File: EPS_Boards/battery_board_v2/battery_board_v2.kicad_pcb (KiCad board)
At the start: 4 copper layers, 90.2 x 95.9 mm, 5 parts, among them J1 PC104_Connector

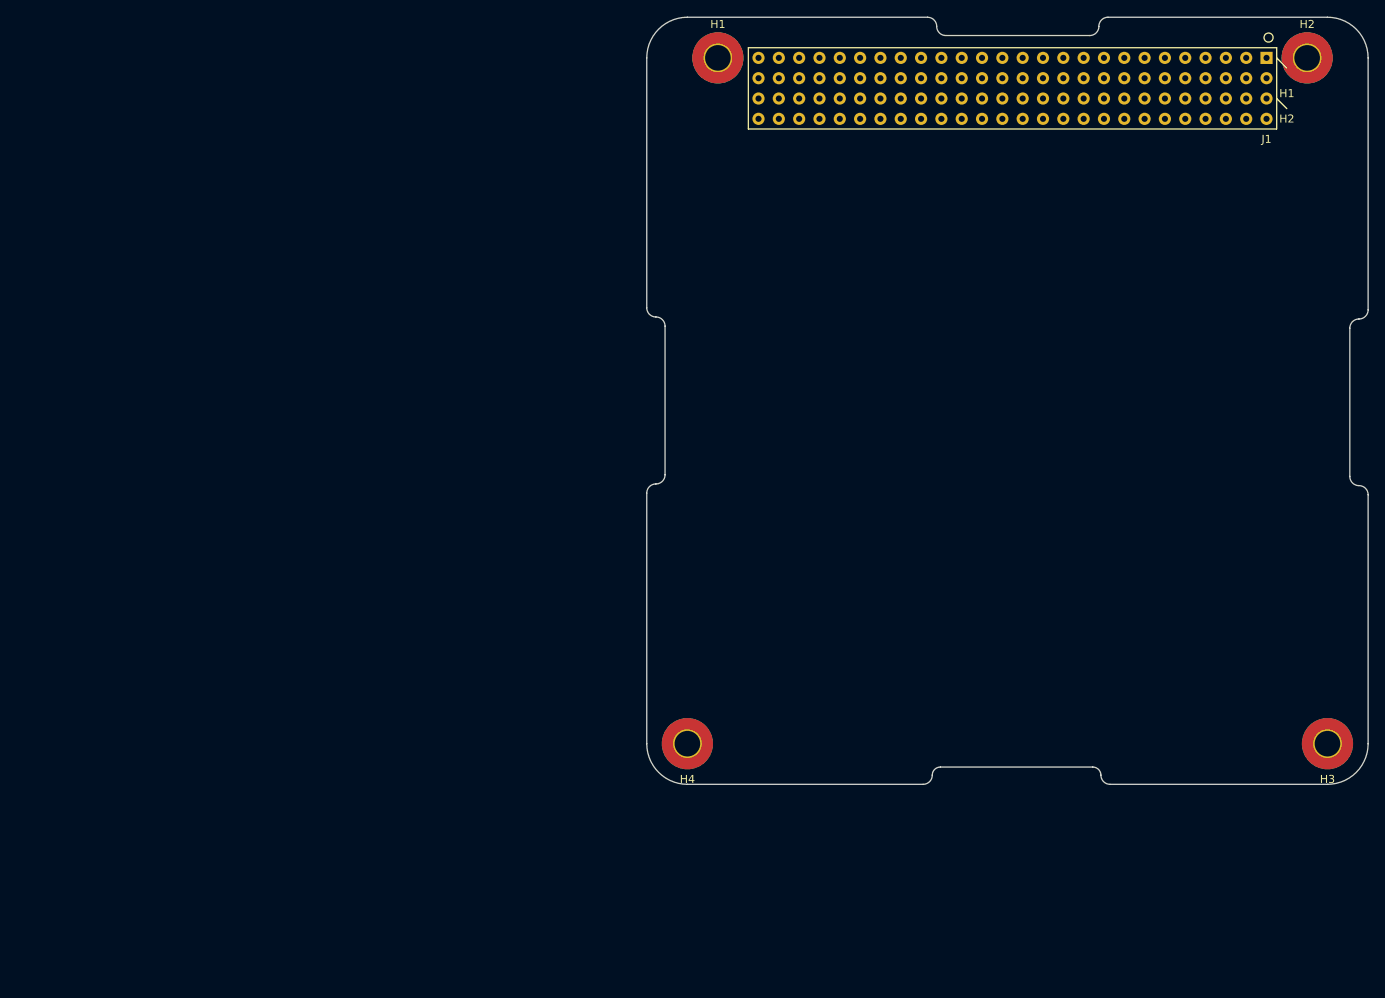
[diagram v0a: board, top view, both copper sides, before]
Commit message: eps: battery board: updated board layout
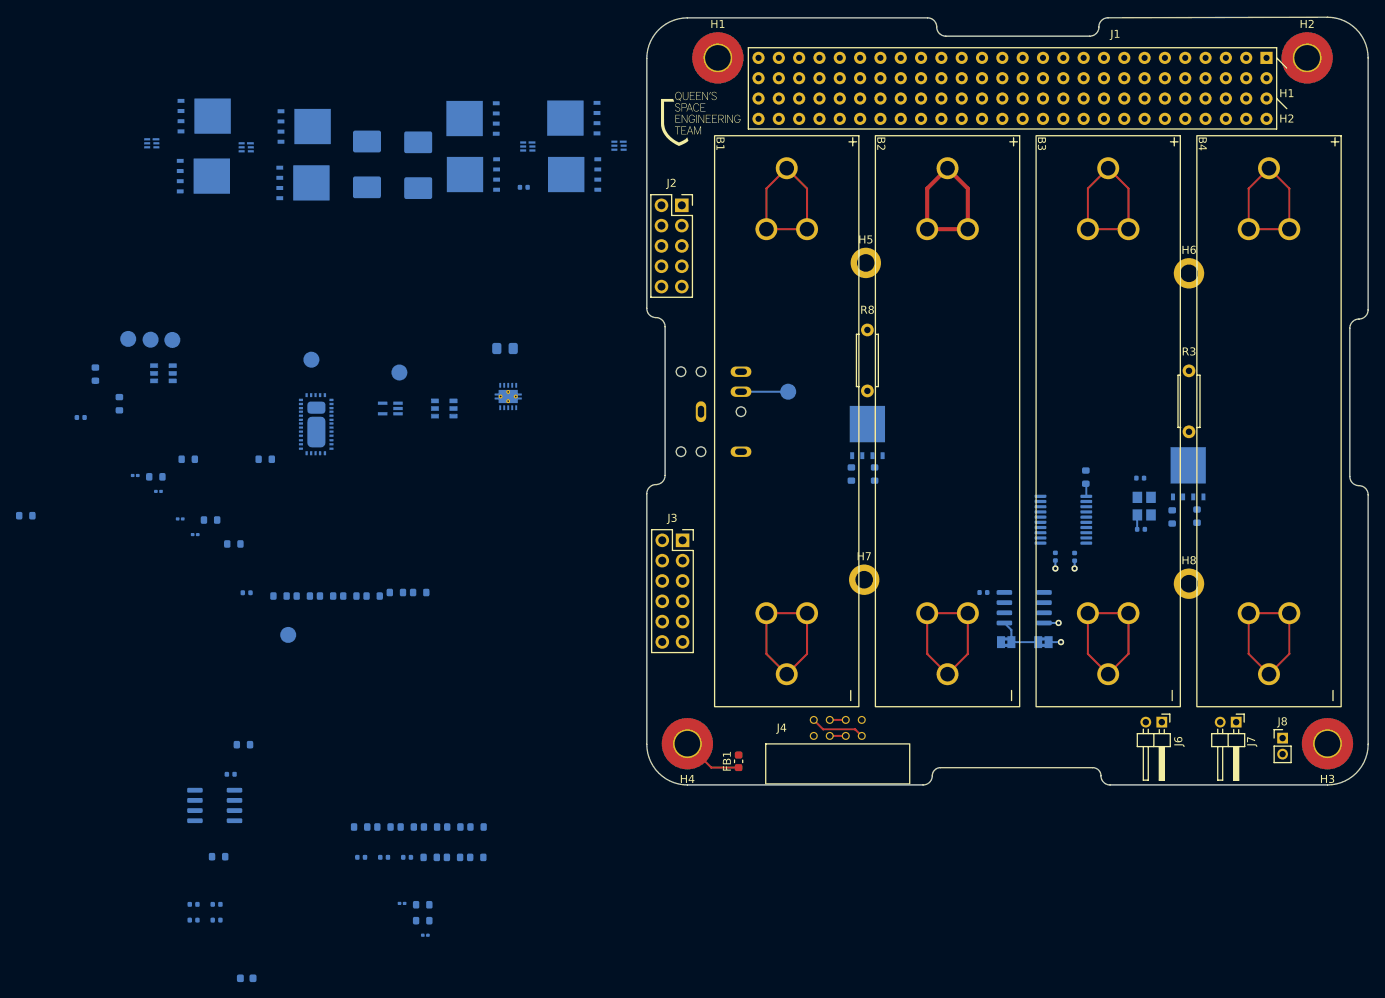
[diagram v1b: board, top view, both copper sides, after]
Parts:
- added B1: NCR18650GA, qset-footprints:Keystone_54_18650, F.Cu at (117.7, 61.8)
- added B2: NCR18650GA, qset-footprints:Keystone_54_18650, F.Cu at (137.8, 61.8)
- added B3: NCR18650GA, qset-footprints:Keystone_54_18650, F.Cu at (157.9, 61.8)
- added B4: NCR18650GA, qset-footprints:Keystone_54_18650, F.Cu at (178.0, 61.8)
- added C1: 0.1u, Capacitor_SMD:C_0402_1005Metric, B.Cu at (151.3, 118.9)
- added C10: 0.1u, Capacitor_SMD:C_0201_0603Metric, B.Cu at (48.2, 106.3)
- added C11: 0.1u, Capacitor_SMD:C_0402_1005Metric, B.Cu at (59.2, 118.9)
- added C12: C, Capacitor_SMD:C_0201_0603Metric, B.Cu at (45.3, 104.3)
- added C13: 0.1u, Capacitor_SMD:C_0201_0603Metric, B.Cu at (50.9, 109.7)
- added C14: 0.1u, Capacitor_SMD:C_0402_1005Metric, B.Cu at (38.5, 97.0)
- added C15: 0.1u, Capacitor_SMD:C_0201_0603Metric, B.Cu at (52.8, 111.7)
- added C16: 0.1u, Capacitor_SMD:C_0402_1005Metric, B.Cu at (76.4, 152.0)
- added C17: 0.1u, Capacitor_SMD:C_0402_1005Metric, B.Cu at (93.8, 68.2)
- added C18: 0.1u, Capacitor_SMD:C_0402_1005Metric, B.Cu at (73.5, 152.0)
- added C19: 0.1u, Capacitor_SMD:C_0402_1005Metric, B.Cu at (79.3, 152.0)
- added C2: 10p, Capacitor_SMD:C_0402_1005Metric, B.Cu at (170.9, 104.6)
- added C20: 0.1u, Capacitor_SMD:C_0402_1005Metric, B.Cu at (57.2, 141.6)
- added C21: 0.1u, Capacitor_SMD:C_0201_0603Metric, B.Cu at (81.5, 161.7)
- added C22: 22n, Capacitor_SMD:C_0201_0603Metric, B.Cu at (78.6, 157.8)
- added C3: 100u, Capacitor_SMD:C_0402_1005Metric, B.Cu at (55.4, 159.8)
- added C4: 10p, Capacitor_SMD:C_0402_1005Metric, B.Cu at (171.0, 111.0)
- added C5: 10u, Capacitor_SMD:C_0402_1005Metric, B.Cu at (160.3, 114.4)
- added C6: 100n, Capacitor_SMD:C_0402_1005Metric, B.Cu at (162.7, 114.4)
- added C7: 10n, Capacitor_SMD:C_0402_1005Metric, B.Cu at (55.4, 157.9)
- added C8: 1u, Capacitor_SMD:C_0402_1005Metric, B.Cu at (52.6, 159.8)
- added C9: 1u, Capacitor_SMD:C_0402_1005Metric, B.Cu at (52.6, 157.9)
- added F1: Polyfuse, Capacitor_Tantalum_SMD:CP_EIA-7132-20_AVX-U_Pad2.72x3.50mm_HandSolder, B.Cu at (80.7, 65.5)
- added F2: Polyfuse, Capacitor_Tantalum_SMD:CP_EIA-7132-20_AVX-U_Pad2.72x3.50mm_HandSolder, B.Cu at (74.2, 65.4)
- added FB1: FerriteBead, Inductor_SMD:L_0603_1608Metric, F.Cu at (120.7, 140.0)
- added FB2: 100R @ 100MHz, Inductor_SMD:L_0603_1608Metric, B.Cu at (59.2, 167.1)
- added G***: LOGO, qset-footprints:Logo-10mm, F.Cu at (116.0, 59.6)
- added H5: MountingHole, MountingHole:MountingHole_2.2mm_M2_DIN965_Pad, F.Cu at (136.6, 77.7)
- added H6: MountingHole, MountingHole:MountingHole_2.2mm_M2_DIN965_Pad, F.Cu at (177.0, 79.0)
- added H7: MountingHole, MountingHole:MountingHole_2.2mm_M2_DIN965_Pad, F.Cu at (136.4, 117.3)
- added H8: MountingHole, MountingHole:MountingHole_2.2mm_M2_DIN965_Pad, F.Cu at (177.0, 117.8)
- added J2: Programming Header, Connector_PinSocket_2.54mm:PinSocket_2x05_P2.54mm_Vertical, F.Cu at (113.6, 70.5)
- added J3: System Test Connector, Connector_PinSocket_2.54mm:PinSocket_2x06_P2.54mm_Vertical, F.Cu at (113.7, 112.4)
- added J4: Conn_01x08_Male, qset-footprints:M80-5300842, F.Cu at (124.1, 142.8)
- added J5: RBF, qset-footprints:CUI_SJ1-3524NG, B.Cu at (116.0, 96.3)
- added J6: RBF Deployment Bypass, Connector_PinHeader_2.00mm:PinHeader_1x02_P2.00mm_Horizontal, F.Cu at (173.6, 135.1)
- added J7: 30s Timer, Connector_PinHeader_2.00mm:PinHeader_1x02_P2.00mm_Horizontal, F.Cu at (182.9, 135.1)
- added J8: Shunt Resistor, Connector_PinHeader_2.00mm:PinHeader_1x02_P2.00mm_Vertical, F.Cu at (188.7, 137.1)
- added L1: 2.2uH, Inductor_SMD:L_0805_2012Metric_Pad1.15x1.40mm_HandSolder, B.Cu at (91.5, 88.4)
- added Q1: CSD16401Q5, Package_TO_SOT_SMD:TDSON-8-1, B.Cu at (176.9, 104.0)
- added Q10: CSD16401Q5, Package_TO_SOT_SMD:TDSON-8-1, B.Cu at (53.8, 66.8)
- added Q2: CSD16401Q5, Package_TO_SOT_SMD:TDSON-8-1, B.Cu at (136.8, 98.9)
- added Q3: CSD16401Q5, Package_TO_SOT_SMD:TDSON-8-1, B.Cu at (100.2, 66.7)
- added Q4: CSD16401Q5, Package_TO_SOT_SMD:TDSON-8-1, B.Cu at (87.5, 66.7)
- added Q5: CSD16401Q5, Package_TO_SOT_SMD:TDSON-8-1, B.Cu at (100.1, 59.6)
- added Q6: CSD16401Q5, Package_TO_SOT_SMD:TDSON-8-1, B.Cu at (87.5, 59.6)
- added Q7: CSD16401Q5, Package_TO_SOT_SMD:TDSON-8-1, B.Cu at (66.4, 60.6)
- added Q8: CSD16401Q5, Package_TO_SOT_SMD:TDSON-8-1, B.Cu at (53.9, 59.4)
- added Q9: CSD16401Q5, Package_TO_SOT_SMD:TDSON-8-1, B.Cu at (66.2, 67.7)
- added R1: 100, Resistor_SMD:R_0603_1608Metric, B.Cu at (178.0, 109.3)
- added R10: 412k, Resistor_SMD:R_0603_1608Metric, B.Cu at (54.7, 109.8)
- added R11: 1M, Resistor_SMD:R_0603_1608Metric, B.Cu at (80.8, 118.9)
- added R12: 390k, Resistor_SMD:R_0603_1608Metric, B.Cu at (57.6, 112.8)
- added R13: ?R, Resistor_SMD:R_0603_1608Metric, B.Cu at (31.6, 109.3)
- added R14: 1M, Resistor_SMD:R_0603_1608Metric, B.Cu at (69.2, 119.3)
- added R15: 887k, Resistor_SMD:R_0603_1608Metric, B.Cu at (51.9, 102.2)
- added R16: 0R, Resistor_SMD:R_0603_1608Metric, B.Cu at (66.3, 119.3)
- added R17: DNP, Resistor_SMD:R_0603_1608Metric, B.Cu at (77.9, 118.9)
- added R18: 100k, Resistor_SMD:R_0603_1608Metric, B.Cu at (72.1, 119.3)
- added R19: 100k, Resistor_SMD:R_0603_1608Metric, B.Cu at (43.3, 95.3)
- added R2: 10k, Resistor_SMD:R_0603_1608Metric, B.Cu at (174.9, 109.5)
- added R20: 560k, Resistor_SMD:R_0603_1608Metric, B.Cu at (61.5, 102.2)
- added R21: 100k, Resistor_SMD:R_0603_1608Metric, B.Cu at (47.9, 104.4)
- added R22: 100k, Resistor_SMD:R_0603_1608Metric, B.Cu at (75.0, 119.3)
- added R23: 270k, Resistor_SMD:R_0603_1608Metric, B.Cu at (40.3, 91.6)
- added R24: 100k, Resistor_SMD:R_0603_1608Metric, B.Cu at (63.4, 119.3)
- added R25: 330, Resistor_SMD:R_0603_1608Metric, B.Cu at (73.5, 148.2)
- added R26: 330, Resistor_SMD:R_0603_1608Metric, B.Cu at (79.3, 148.2)
- added R27: 2.2k, Resistor_SMD:R_0603_1608Metric, B.Cu at (82.2, 152.0)
- added R28: 2.2k, Resistor_SMD:R_0603_1608Metric, B.Cu at (88.0, 148.2)
- added R29: 0.1, Resistor_SMD:R_0603_1608Metric, B.Cu at (76.4, 148.2)
- added R3: 100, Resistor_THT:R_Axial_DIN0207_L6.3mm_D2.5mm_P7.62mm_Horizontal, F.Cu at (177.0, 98.8)
- added R30: 2.2k, Resistor_SMD:R_0603_1608Metric, B.Cu at (88.0, 152.0)
- added R31: 2.2k, Resistor_SMD:R_0603_1608Metric, B.Cu at (85.1, 152.0)
- added R32: 330, Resistor_SMD:R_0603_1608Metric, B.Cu at (85.1, 148.2)
- added R33: 330, Resistor_SMD:R_0603_1608Metric, B.Cu at (82.2, 148.2)
- added R34: 3.3k, Resistor_SMD:R_0603_1608Metric, B.Cu at (58.8, 137.9)
- added R35: 3.3k, Resistor_SMD:R_0603_1608Metric, B.Cu at (55.7, 151.9)
- added R36: 10k, Resistor_SMD:R_0603_1608Metric, B.Cu at (81.2, 157.9)
- added R37: 1k, Resistor_SMD:R_0603_1608Metric, B.Cu at (81.2, 159.9)
- added R4: 0R, Jumper:SolderJumper-2_P1.3mm_Bridged2Bar_Pad1.0x1.5mm, B.Cu at (154.2, 125.1)
- added R5: 0R, Jumper:SolderJumper-2_P1.3mm_Bridged2Bar_Pad1.0x1.5mm, B.Cu at (158.8, 125.1)
- added R6: 100, Resistor_SMD:R_0603_1608Metric, B.Cu at (137.7, 104.1)
- added R7: 10k, Resistor_SMD:R_0603_1608Metric, B.Cu at (134.8, 104.1)
- added R8: 100, Resistor_THT:R_Axial_DIN0207_L6.3mm_D2.5mm_P7.62mm_Horizontal, F.Cu at (136.8, 93.7)
- added R9: 10k, Resistor_SMD:R_0603_1608Metric, B.Cu at (164.1, 104.5)
- added TP1: Deployment TP, TestPoint:TestPoint_Pad_D2.0mm, B.Cu at (126.9, 93.8)
- added TP2: Power Control TP, TestPoint:TestPoint_Pad_D2.0mm, B.Cu at (44.4, 87.2)
- added TP3: EN_D3, TestPoint:TestPoint_Pad_D2.0mm, B.Cu at (78.3, 91.4)
- added TP4: Timer, TestPoint:TestPoint_Pad_D2.0mm, B.Cu at (47.2, 87.3)
- added TP5: HB, TestPoint:TestPoint_Pad_D2.0mm, B.Cu at (64.4, 124.2)
- added TP6: EN_D1, TestPoint:TestPoint_Pad_D2.0mm, B.Cu at (67.3, 89.8)
- added TP7: HB Reset, TestPoint:TestPoint_Pad_D2.0mm, B.Cu at (49.9, 87.3)
- added U1: TMP36xS, Package_SO:SOIC-8_3.9x4.9mm_P1.27mm, B.Cu at (156.4, 120.8)
- added U10: BQ297xx, Package_SON:WSON-6_1.5x1.5mm_P0.5mm, B.Cu at (59.1, 63.2)
- added U11: BQ297xx, Package_SON:WSON-6_1.5x1.5mm_P0.5mm, B.Cu at (47.4, 62.8)
- added U12: INA219AxD, Package_SO:SOIC-8_3.9x4.9mm_P1.27mm, B.Cu at (55.2, 145.5)
- added U13: TPS24750, qset-footprints:TPS24750, B.Cu at (67.7, 98.1)
- added U2: STM32F030F4Px, Package_SO:TSSOP-20_4.4x6.5mm_P0.65mm, B.Cu at (161.3, 109.8)
- added U3: TPS63000-Q1, Package_SON:Texas_DRC0010J_ThermalVias, B.Cu at (91.9, 94.4)
- added U4: LTC6995HS6-1#TRMPBF, qset-footprints:SOT95P280X100-6N, B.Cu at (83.9, 95.9)
- added U5: LTC6995HS6-1#TRMPBF, qset-footprints:SOT95P280X100-6N, B.Cu at (48.8, 91.5)
- added U6: 74AUP1G08, qset-footprints:SOT65P210X110-5N, B.Cu at (77.2, 95.9)
- added U8: BQ297xx, Package_SON:WSON-6_1.5x1.5mm_P0.5mm, B.Cu at (105.8, 63.0)
- added U9: BQ297xx, Package_SON:WSON-6_1.5x1.5mm_P0.5mm, B.Cu at (94.3, 63.1)
- added Y1: 16 MHz, Crystal:Crystal_SMD_3225-4Pin_3.2x2.5mm, B.Cu at (171.4, 108.1)
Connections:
- H1 pad 1: unconnected-(H1-Pad1) -> Net-(FB1-Pad1)
- H2 pad 1: unconnected-(H2-Pad1) -> Net-(FB1-Pad1)
- H3 pad 1: unconnected-(H3-Pad1) -> Net-(FB1-Pad1)
- H4 pad 1: unconnected-(H4-Pad1) -> Net-(FB1-Pad1)
- J1 pad 100: unconnected-(J1-Pad100) -> GND
- J1 pad 32: unconnected-(J1-Pad32) -> 5V_USB_CHG
- J1 pad 41: unconnected-(J1-Pad41) -> I2C_DATA
- J1 pad 43: unconnected-(J1-Pad43) -> I2C_CLK
- J1 pad 61: unconnected-(J1-Pad61) -> GND
- J1 pad 66: unconnected-(J1-Pad66) -> GND
- J1 pad 69: unconnected-(J1-Pad69) -> GND
- J1 pad 7: unconnected-(J1-Pad7) -> BAT_INT
- J1 pad 73: unconnected-(J1-Pad73) -> GND
- J1 pad 74: unconnected-(J1-Pad74) -> GND
- J1 pad 77: unconnected-(J1-Pad77) -> 5VBUS
- J1 pad 78: unconnected-(J1-Pad78) -> 5VBUS
- J1 pad 79: unconnected-(J1-Pad79) -> 3V3BUS
- J1 pad 80: unconnected-(J1-Pad80) -> 3V3BUS
- J1 pad 81: unconnected-(J1-Pad81) -> GND
- J1 pad 82: unconnected-(J1-Pad82) -> GND
- J1 pad 84: unconnected-(J1-Pad84) -> GND
- J1 pad 87: unconnected-(J1-Pad87) -> PCM_IN
- J1 pad 88: unconnected-(J1-Pad88) -> PCM_IN
- J1 pad 93: unconnected-(J1-Pad93) -> BCR_OUT
- J1 pad 94: unconnected-(J1-Pad94) -> BCR_OUT
- J1 pad 95: unconnected-(J1-Pad95) -> BCR_OUT
- J1 pad 96: unconnected-(J1-Pad96) -> BCR_OUT
- J1 pad 99: unconnected-(J1-Pad99) -> GND
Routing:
- net IV_MON_N: track 0.00 -> 44.8 mm
- net Net-(B2-Pad2): track 0.00 -> 22.4 mm
- net Net-(B1-Pad2): track 0.00 -> 22.4 mm
- net Net-(B4-Pad2): track 0.00 -> 22.4 mm
- net Net-(B3-Pad2): track 0.00 -> 22.4 mm
- net Net-(B2-Pad1): track 0.00 -> 22.4 mm
- net Net-(B3-Pad1): track 0.00 -> 22.4 mm
- net GND: track 0.00 -> 17.0 mm, vias 0 -> 4
- net Net-(FB1-Pad1): track 0.00 -> 7.64 mm
- net Net-(J4-Pad4): track 0.00 -> 6.83 mm
- net Net-(R4-Pad2): track 0.00 -> 6.11 mm
- net Net-(J5-Pad4): track 0.00 -> 5.90 mm
- net Net-(J4-Pad6): track 0.00 -> 2.00 mm
- net Net-(J4-Pad2): track 0.00 -> 2.00 mm
- net Net-(C4-Pad1): track 0.00 -> 1.81 mm
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- added copper zone on In2.Cu, net 3V3BUS
- added copper zone on In1.Cu, net GND
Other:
- board size 90.2 x 95.9 mm -> 90.2 x 96 mm
- board text added: "Battery Board RevA, 2022-2023 Griffin Jones & Jacob O'Riordan-Ross SN: ____"

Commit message: eps: battery board: dino pic
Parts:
- added G***: LOGO, LOGO, F.Cu at (194.7, 55.7)

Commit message: eps: battery board: more updates to layout
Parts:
- moved U10 198.5 mm to (255.8, 90.3), turned to 0 degrees
- moved C18 195.3 mm to (258.8, 90.2), turned to -90 degrees
- moved Q9 188.3 mm to (253.7, 85.2), turned to 90 degrees
- moved R32 184.8 mm to (260.6, 90.3), turned to -90 degrees
- moved Q7 182.5 mm to (247.2, 85.2), turned to 90 degrees
- moved R30 173.8 mm to (250.6, 90.7)
- moved U11 145.4 mm to (190.3, 89.1), turned to 0 degrees
- moved Q10 136.0 mm to (188.8, 83.5), turned to 90 degrees
- moved R35 132.6 mm to (166.3, 78.8), turned to 90 degrees
- moved Q8 130.0 mm to (181.6, 83.5), turned to 90 degrees
- moved C19 129.8 mm to (193.1, 89.5), turned to -90 degrees
- moved U12 127.2 mm to (166.4, 83.7), turned to 0 degrees
- moved R33 127.0 mm to (194.9, 89.6), turned to -90 degrees
- moved F2 124.5 mm to (181.6, 128.4)
- moved C7 120.6 mm to (154.6, 89.2), turned to -90 degrees
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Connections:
- J1 pad 41: I2C_DATA -> I2C_SDA
- J1 pad 43: I2C_CLK -> I2C_SCK
- R36 pad 1: PACK_NEG -> PACK_N
- U13 pad GND: (no net) -> GND
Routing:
- net IV_MON_N: track 44.8 -> 125.9 mm
- net Net-(B4-Pad2): track 22.4 -> 67.9 mm, vias 0 -> 1
- net SWCLK: track 0.00 -> 32.5 mm
- net GND: track 17.0 -> 49.2 mm, vias 4 -> 24
- net SWDIO: track 0.00 -> 29.8 mm
- net Net-(B3-Pad1): track 22.4 -> 49.7 mm
- net 3V3BUS: track 0.00 -> 16.6 mm, vias 0 -> 8
- net EN_D1: track 0.00 -> 16.5 mm
- net BCR_OUT: track 0.00 -> 12.4 mm
- net BAT_TEMP: track 0.00 -> 12.3 mm
- net Net-(Q6-Pad4): track 0.00 -> 12.1 mm
- net Net-(Q5-Pad4): track 0.00 -> 11.9 mm
- net Net-(Q8-Pad4): track 0.00 -> 11.8 mm
- net Net-(Q7-Pad4): track 0.00 -> 11.5 mm
- net BAT_INT: track 0.00 -> 10.1 mm
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
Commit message: eps: battery board: progress on pcb layout
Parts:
- moved C13 194.1 mm to (212.9, 92.5)
- moved C15 192.2 mm to (213.1, 95.6)
- moved R24 184.6 mm to (213.1, 98.8)
- moved TP5 172.3 mm to (204.8, 98.8)
- moved U13 134.0 mm to (167.6, 113.0), turned to -90 degrees
- moved R22 132.8 mm to (176.8, 148.0)
- moved TP7 132.6 mm to (204.8, 93.8)
- moved R37 130.8 mm to (164.1, 112.0)
- moved C22 130.3 mm to (170.9, 108.7), turned to -90 degrees
- moved TP3 128.7 mm to (172.8, 146.7)
- moved R18 126.4 mm to (179.3, 149.4), turned to 0 degrees
- moved R10 126.2 mm to (184.3, 152.8)
- moved U4 124.7 mm to (178.4, 152.2)
- moved TP6 122.0 mm to (163.2, 107.5)
- moved C10 117.3 mm to (173.6, 150.4)
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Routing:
- net EN_D1: track 16.5 -> 7.70 mm
- net Net-(Q7-Pad5): track 6.52 -> 0.00 mm
- net Net-(R23-Pad2): track 0.00 -> 5.53 mm
- net Net-(R23-Pad1): track 0.00 -> 3.81 mm
- net Net-(F2-Pad1): track 8.68 -> 5.83 mm
- net nRST_HB: track 0.00 -> 2.11 mm
- net Net-(C22-Pad1): track 2.11 -> 0.14 mm
- net Net-(C17-Pad2): track 4.42 -> 3.53 mm
- net Net-(Q7-Pad4): track 11.5 -> 12.3 mm

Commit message: eps: battery board: worked on traces
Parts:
- moved R36 99.9 mm to (209.6, 124.5)
- moved R35 13.0 mm to (164.1, 90.2), turned to -90 degrees
- moved R34 12.5 mm to (162.2, 90.3), turned to -90 degrees
- moved C20 9.12 mm to (162.7, 80.0), turned to 180 degrees
- moved Q7 7.83 mm to (188.1, 101.0)
- moved R29 7.64 mm to (166.1, 79.2), turned to 180 degrees
- moved F1 6.96 mm to (166.3, 132.6), turned to 0 degrees
- moved Q9 5.48 mm to (188.2, 107.3)
- moved R30 2.79 mm to (194.5, 107.8)
- moved U12 2.41 mm to (164.1, 84.4), turned to 90 degrees
- moved U10 1.98 mm to (193.8, 101.8)
- moved R21 0.61 mm to (149.6, 110.2)
- moved R37 0.23 mm to (163.9, 112.0)
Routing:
- net GND: track 49.3 -> 64.0 mm, vias 24 -> 22
- net Net-(F2-Pad1): track 5.83 -> 19.6 mm
- net Net-(B3-Pad1): track 49.7 -> 62.2 mm
- net Net-(Q7-Pad4): track 12.3 -> 0.25 mm
- net Net-(Q7-Pad5): track 0.00 -> 6.36 mm
- net Net-(B3-Pad2): track 29.4 -> 34.5 mm
- net 3V3_CON: track 0.00 -> 4.63 mm
- net Net-(R20-Pad2): track 0.00 -> 4.25 mm
- net Net-(R16-Pad2): track 0.00 -> 3.99 mm
- net Net-(Q9-Pad4): track 4.18 -> 8.00 mm
- net Net-(J6-Pad1): track 0.00 -> 3.22 mm
- net Net-(L1-Pad2): track 0.00 -> 3.09 mm
- net BCR_OUT: track 12.4 -> 15.5 mm
- net Net-(L1-Pad1): track 0.00 -> 3.05 mm
- net IV_MON_N: track 125.9 -> 128.8 mm
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
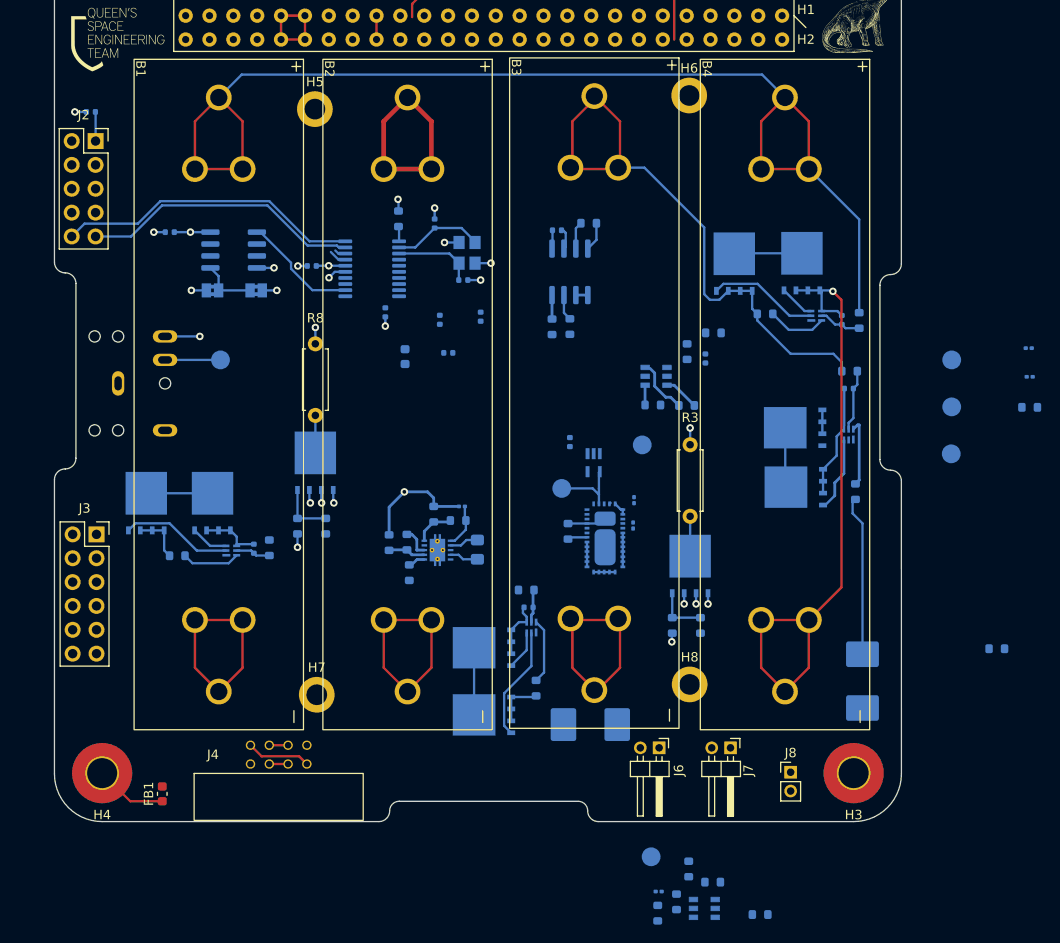
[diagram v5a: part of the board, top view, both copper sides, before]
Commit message: eps: battery board: more traces
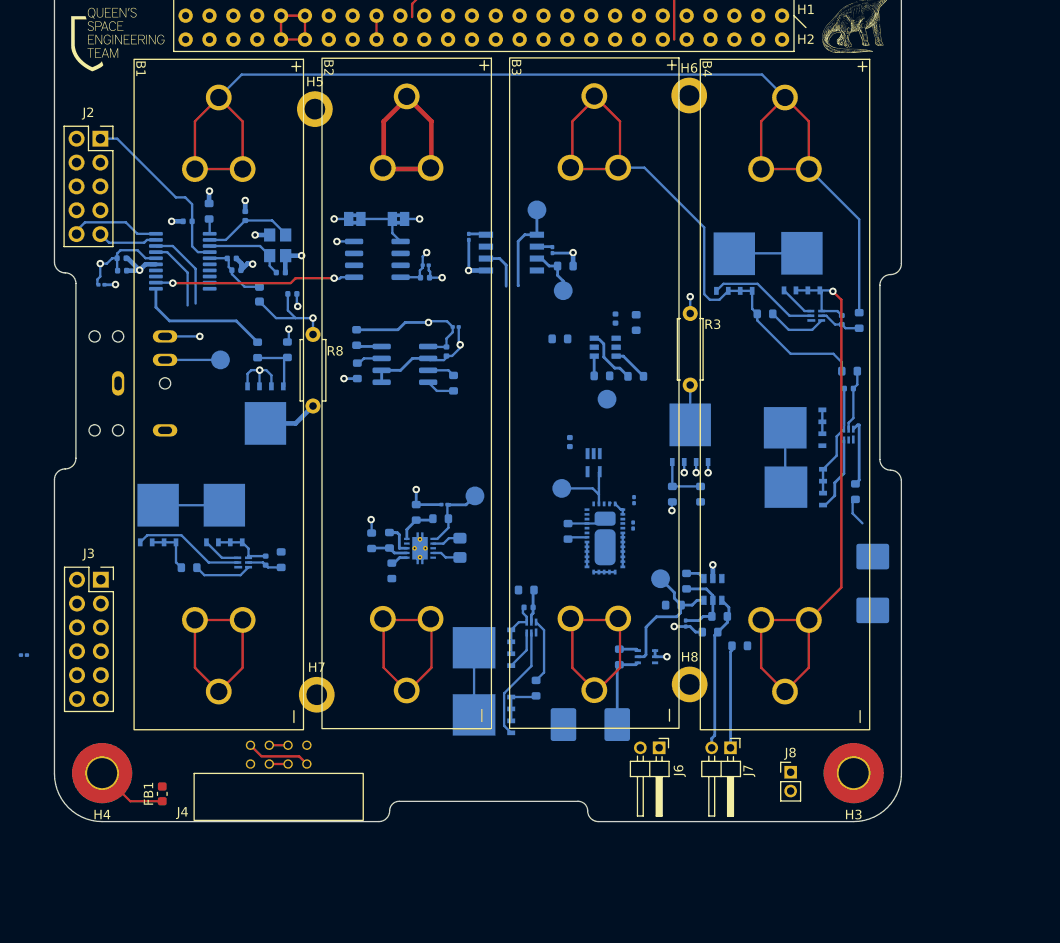
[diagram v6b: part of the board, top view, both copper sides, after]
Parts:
- added D1: DESD3V3E1BL-7B, Resistor_SMD:R_0201_0603Metric, B.Cu at (148.8, 83.7)
- added D2: DESD3V3E1BL-7B, Resistor_SMD:R_0201_0603Metric, B.Cu at (114.2, 85.8)
- added D3: DESD3V3E1BL-7B, Resistor_SMD:R_0201_0603Metric, B.Cu at (106.0, 125.2)
- added D4: DESD3V3E1BL-7B, Resistor_SMD:R_0201_0603Metric, B.Cu at (151.9, 90.3)
- added Q11: NTJD1155LT1G, qset-footprints:TRANS_NTJD1155LT1G, B.Cu at (172.2, 125.4)
- added U7: UCC2946D, qset-footprints:SOIC127P600X175-8N, B.Cu at (157.9, 82.4)
- moved C13 60.8 mm to (153.3, 80.7), turned to -90 degrees
- moved C15 52.6 mm to (162.2, 82.1), turned to -90 degrees
- moved R24 51.7 mm to (163.6, 83.8), turned to 0 degrees
- moved TP2 50.9 mm to (154.0, 108.3)
- moved TP7 47.0 mm to (160.6, 77.8)
- moved TP5 43.2 mm to (163.4, 86.4)
- moved R36 40.2 mm to (169.4, 125.4), turned to 90 degrees
- moved U4 34.0 mm to (179.3, 118.2), turned to -90 degrees
- moved R18 32.2 mm to (176.5, 117.4), turned to 90 degrees
- moved R14 30.7 mm to (180.0, 121.1), turned to 0 degrees
- moved R15 30.4 mm to (179.0, 122.8), turned to 180 degrees
- moved TP3 29.6 mm to (173.8, 117.1), turned to -90 degrees
- moved R10 28.7 mm to (182.2, 124.2), turned to 0 degrees
- moved C10 28.7 mm to (176.4, 121.9), turned to -90 degrees
- moved C6 28.4 mm to (116.4, 84.3), turned to 0 degrees
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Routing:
- net 3V3BUS: track 14.0 -> 47.5 mm, vias 5 -> 7
- net GND: track 64.0 -> 94.7 mm, vias 22 -> 27
- net SWDIO: track 29.8 -> 6.41 mm
- net SWCLK: track 32.5 -> 9.69 mm
- net Net-(J7-Pad2): track 0.00 -> 16.8 mm
- net NRST: track 3.12 -> 19.3 mm
- net EN_D3: track 0.00 -> 15.4 mm
- net BAT_HTR_2: track 0.00 -> 14.3 mm
- net Net-(F2-Pad1): track 19.6 -> 5.65 mm
- net 3V3_CON: track 4.63 -> 16.3 mm
- net Net-(J7-Pad1): track 0.00 -> 10.5 mm
- net nRST_HB: track 2.11 -> 11.8 mm
- net BAT_TEMP: track 12.3 -> 21.6 mm, vias 0 -> 2
- net PACK_N: track 0.00 -> 8.52 mm
- net I2C_SDA: track 3.99 -> 11.7 mm
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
